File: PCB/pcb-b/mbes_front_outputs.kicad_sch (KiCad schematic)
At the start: 57 parts, among them Q1 BC817, Q10 BC817, Q11 TPCA8120,L1Q, Q14 BC817, Q15 BC817, Q19 BC817, Q2 BC817, Q20 BC817, Q21 BC817, Q4 TPCA8120,L1Q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

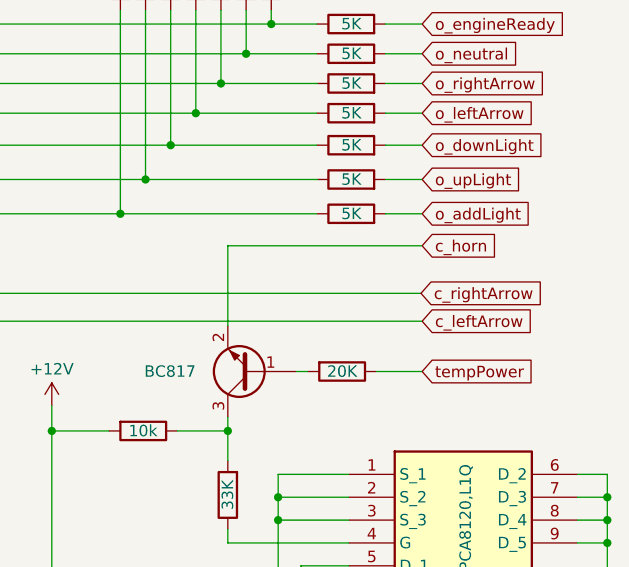
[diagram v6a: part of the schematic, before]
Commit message: Many changes and fixes
Electric schema A & B
	- Wrong (undefined) signals direction fixed
	- More readable schema getting: c_<signal> color has changed
	- Some pull-up resistors has been added for safing purpose
	- Wire connectors holes size reducing
	- Because Led indicatord uses less then 500mA, their wire connectors have been substituted by pin-header ones

PCB
	- Updates for schema changes
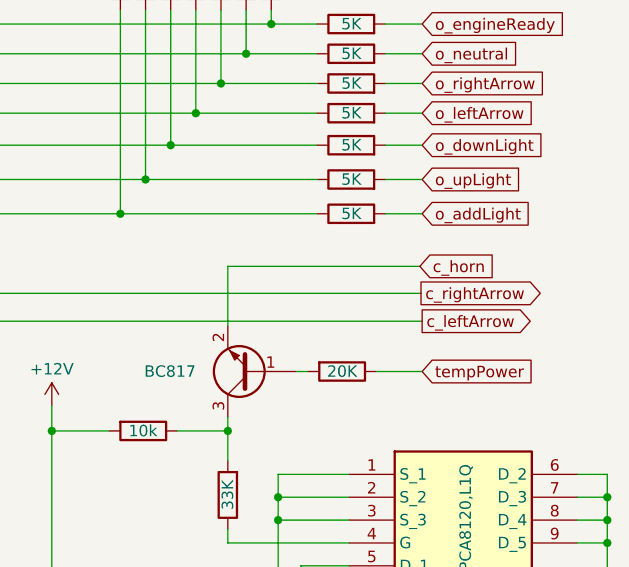
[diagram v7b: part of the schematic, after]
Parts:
- DownLight_p1, addLight_p1: footprint Connector_Wire:SolderWire-1.5sqmm_1x02_P6mm_D1.7mm_OD3mm -> Connector_Wire:SolderWire-0.75sqmm_1x02_P4.8mm_D1.25mm_OD2.3mm
- Horn_p1, UpLight_p1: footprint Connector_Wire:SolderWire-1.5sqmm_1x02_P6mm_D1.7mm_OD3mm -> Connector_Wire:SolderWire-1sqmm_1x02_P5.4mm_D1.4mm_OD2.7mm
- leftArrow_p1, rightArrow_p1: footprint Connector_Wire:SolderWire-0.75sqmm_1x02_P4.8mm_D1.25mm_OD2.3mm -> Connector_PinHeader_2.54mm:PinHeader_1x02_P2.54mm_Vertical
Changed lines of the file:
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@@
 	(wire
 		(pts
-			(xy 196.596 111.76) (xy 218.186 111.76)
+			(xy 196.596 114.046) (xy 217.932 114.046)
 		)
 		(stroke
@@
 	(wire
 		(pts
-			(xy 196.596 111.76) (xy 196.596 120.65)
+			(xy 196.596 114.046) (xy 196.596 120.65)
 		)
 		(stroke
@@
 	)
 	(global_label "c_rightArrow"
-		(shape input)
+		(shape output)
 		(at 218.059 117.0432 0)
 		(fields_autoplaced yes)
@@
 			(font
 				(size 1.27 1.27)
+				(color 221 133 0 1)
 			)
 			(justify left)
@@
 	(global_label "c_horn"
 		(shape input)
-		(at 218.186 111.76 0)
+		(at 217.932 114.046 0)
 		(fields_autoplaced yes)
 		(effects
 			(font
 				(size 1.27 1.27)
+				(color 221 133 0 1)
 			)
 			(justify left)
 		)
 		(property "Intersheetrefs" "${INTERSHEET_REFS}"
-			(at 227.4606 111.76 0)
+			(at 227.2066 114.046 0)
 			(effects
 				(font
@@
 		)
 		(property "Riferimenti inter-foglio" "${INTERSHEET_REFS}"
-			(at 218.186 113.9508 0)
+			(at 217.932 116.2368 0)
 			(effects
 				(font
@@
 	)
 	(global_label "c_leftArrow"
-		(shape input)
+		(shape output)
 		(at 218.186 120.142 0)
 		(fields_autoplaced yes)
@@
 			(font
 				(size 1.27 1.27)
+				(color 221 133 0 1)
 			)
 			(justify left)
@@
 			)
 		)
-		(property "Footprint" "Connector_Wire:SolderWire-0.75sqmm_1x02_P4.8mm_D1.25mm_OD2.3mm"
+		(property "Footprint" "Connector_PinHeader_2.54mm:PinHeader_1x02_P2.54mm_Vertical"
 			(at 124.968 176.784 0)
 			(effects
@@
 			)
 		)
-		(property "Footprint" "Connector_Wire:SolderWire-1.5sqmm_1x02_P6mm_D1.7mm_OD3mm"
+		(property "Footprint" "Connector_Wire:SolderWire-0.75sqmm_1x02_P4.8mm_D1.25mm_OD2.3mm"
 			(at 86.5632 176.1744 0)
 			(effects
@@
 			)
 		)
-		(property "Footprint" "Connector_Wire:SolderWire-1.5sqmm_1x02_P6mm_D1.7mm_OD3mm"
+		(property "Footprint" "Connector_Wire:SolderWire-1sqmm_1x02_P5.4mm_D1.4mm_OD2.7mm"
 			(at 202.184 161.036 0)
 			(effects
@@
 			)
 		)
-		(property "Footprint" "Connector_Wire:SolderWire-1.5sqmm_1x02_P6mm_D1.7mm_OD3mm"
+		(property "Footprint" "Connector_Wire:SolderWire-1sqmm_1x02_P5.4mm_D1.4mm_OD2.7mm"
 			(at 61.6204 176.1744 0)
 			(effects
@@
 			)
 		)
-		(property "Footprint" "Connector_Wire:SolderWire-0.75sqmm_1x02_P4.8mm_D1.25mm_OD2.3mm"
+		(property "Footprint" "Connector_PinHeader_2.54mm:PinHeader_1x02_P2.54mm_Vertical"
 			(at 114.808 177.038 0)
 			(effects
@@
 			)
 		)
-		(property "Footprint" "Connector_Wire:SolderWire-1.5sqmm_1x02_P6mm_D1.7mm_OD3mm"
+		(property "Footprint" "Connector_Wire:SolderWire-0.75sqmm_1x02_P4.8mm_D1.25mm_OD2.3mm"
 			(at 30.5054 176.3522 0)
 			(effects

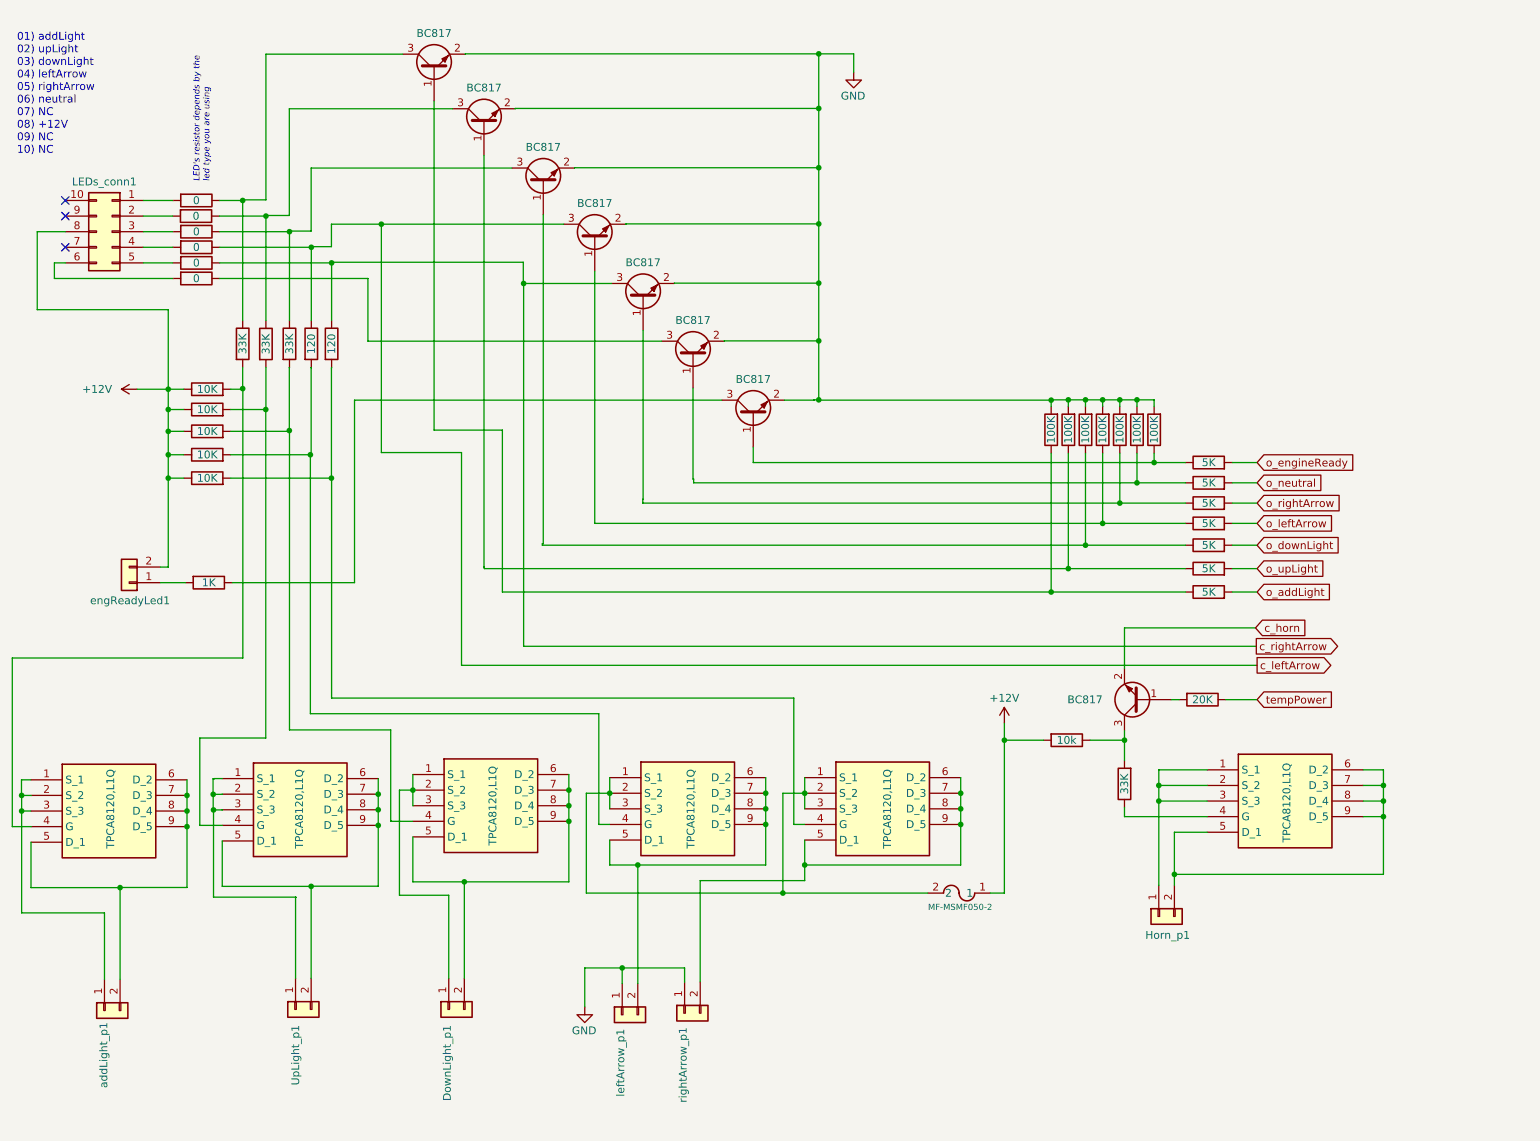
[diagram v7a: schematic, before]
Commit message: Enhancements and size reduction
- Because the day-light needs just low current (<=500 mA), it no more uses the passive fuse. It has been replaced by a
  MSMF050-2 electronic fuse. Less passive fuses means less electric wires, then less chaos!
- A better components space distribution has reduced the PCB size (40.00mm x 90.11mm)
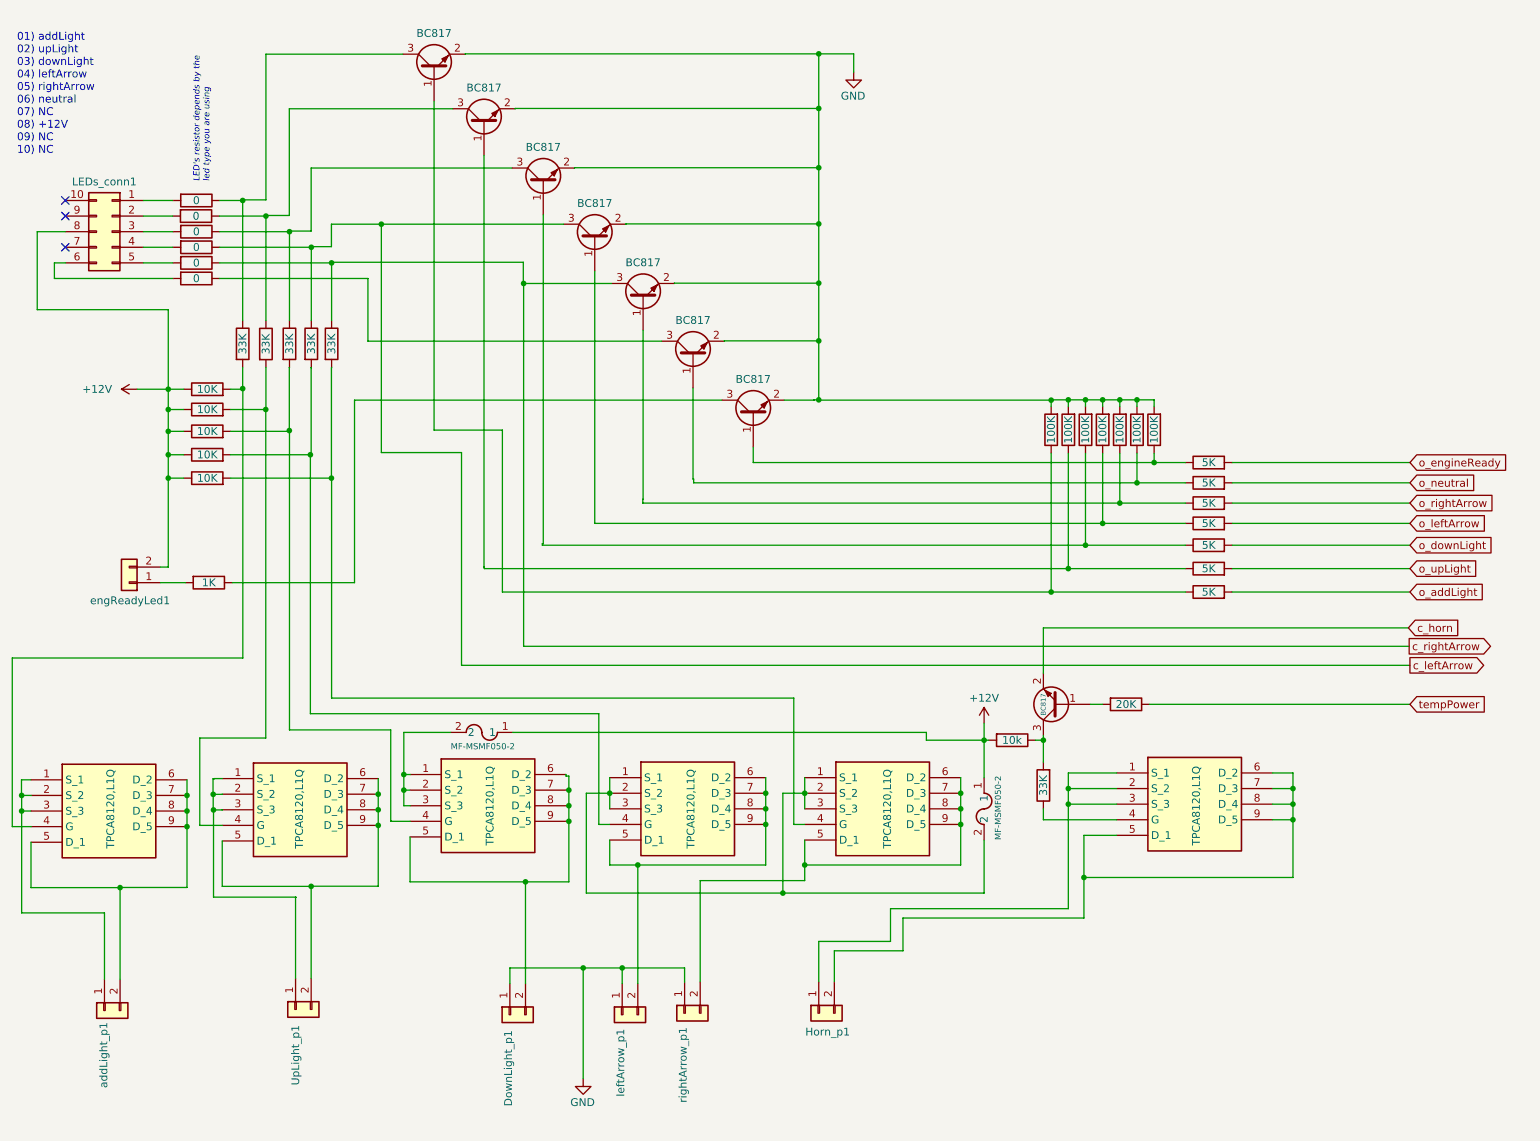
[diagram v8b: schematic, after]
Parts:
- added F1: MF-MSMF050-2, MF-MSMF050-2:FUSE_F050-2, symbol MSMF050-2:MF-MSMF050-2
- DownLight_p1: footprint Connector_Wire:SolderWire-0.75sqmm_1x02_P4.8mm_D1.25mm_OD2.3mm -> Connector_PinHeader_2.54mm:PinHeader_1x02_P2.54mm_Vertical
- F2: footprint MSMF050-2:FUSE_F050-2 -> MF-MSMF050-2:FUSE_F050-2
- RA13, RA14: value 120 -> 33K
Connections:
- net +12V: now also F1.1
- net GND: now also DownLight_p1.1 (Pin_1)
- net at Q5.1 (S_1), Q5.2 (S_2), Q5.3 (S_3): now also F1.2; no longer DownLight_p1.1 (Pin_1)
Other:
- company: (none) -> https://github.com/catinella/mbElectricalSystem
- title: (none) -> Power stage
- moved on the sheet: DownLight_p1, Horn_p1
